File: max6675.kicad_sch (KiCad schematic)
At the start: 14 parts, among them J3 Conn_01x02_Socket, U3 AP2127R-3.3, U5 MAX31855KASA

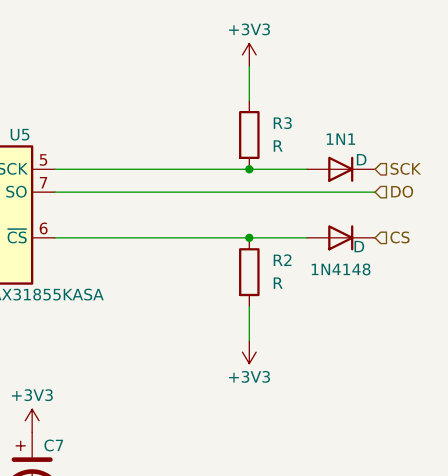
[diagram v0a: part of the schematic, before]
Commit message: adds labels
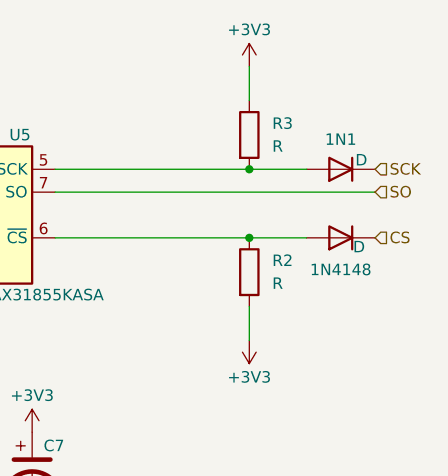
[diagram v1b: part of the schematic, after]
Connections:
- net DO renamed SO
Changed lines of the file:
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@@
 		)
 	)
-	(hierarchical_label "DO"
+	(hierarchical_label "SO"
 		(shape input)
 		(at 120.65 43.18 0)
@@
 					(unit 1)
 				)
+				(path "/a037544f-9a20-478c-bac0-d162f9edf245/ee4cde56-c1fa-403c-8798-e93040e5410a"
+					(reference "#PWR017")
+					(unit 1)
+				)
 			)
 		)
@@
 					(unit 1)
 				)
+				(path "/a037544f-9a20-478c-bac0-d162f9edf245/ee4cde56-c1fa-403c-8798-e93040e5410a"
+					(reference "FB3")
+					(unit 1)
+				)
 			)
 		)
@@
 					(unit 1)
 				)
+				(path "/a037544f-9a20-478c-bac0-d162f9edf245/ee4cde56-c1fa-403c-8798-e93040e5410a"
+					(reference "#PWR018")
+					(unit 1)
+				)
 			)
 		)
@@
 					(unit 1)
 				)
+				(path "/a037544f-9a20-478c-bac0-d162f9edf245/ee4cde56-c1fa-403c-8798-e93040e5410a"
+					(reference "U5")
+					(unit 1)
+				)
 			)
 		)
@@
 					(unit 1)
 				)
+				(path "/a037544f-9a20-478c-bac0-d162f9edf245/ee4cde56-c1fa-403c-8798-e93040e5410a"
+					(reference "C9")
+					(unit 1)
+				)
 			)
 		)
@@
 				(path "/a037544f-9a20-478c-bac0-d162f9edf245/1bf4faff-0fe0-485e-b99b-582bd0fd1695"
 					(reference "#PWR041")
+					(unit 1)
+				)
+				(path "/a037544f-9a20-478c-bac0-d162f9edf245/ee4cde56-c1fa-403c-8798-e93040e5410a"
+					(reference "#PWR019")
 					(unit 1)
 				)
@@
 					(unit 1)
 				)
+				(path "/a037544f-9a20-478c-bac0-d162f9edf245/ee4cde56-c1fa-403c-8798-e93040e5410a"
+					(reference "R3")
+					(unit 1)
+				)
 			)
 		)
@@
 					(unit 1)
 				)
+				(path "/a037544f-9a20-478c-bac0-d162f9edf245/ee4cde56-c1fa-403c-8798-e93040e5410a"
+					(reference "1N1")
+					(unit 1)
+				)
